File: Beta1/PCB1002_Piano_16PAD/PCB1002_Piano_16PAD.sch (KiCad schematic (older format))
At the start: 40 parts, among them U1 MPR121OTS, U2 MPR121OTS, U3 MPR121OTS

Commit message: Removed Kludge connections. Added MPR121 parts. Reannotated.
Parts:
- removed +3.3VA0, +3.3VB0, +3.3VC0, GNDA0, GNDB0, GNDC0, IRQA0, IRQB0, IRQC0, SCLA0, SCLB0, SCLC0, SDAA0, SDAB0, SDAC0: CONN_01X01, Liberry:single_0.1, symbol CONN_01X01
- removed U1, U2, U3: MPR121OTS, Liberry:MPR121OTS, symbol MPR121OTS
- added C1 (x2), C101: CC0603KRX7R9BB104, Capacitors_SMD:C_0603, symbol C
- added C102, C2 (x2): 0.1uf, Capacitors_SMD:C_0603, symbol C
- added P00, P01, P02, P03, P04, P05, P06, P07, P08, P09, P10, P100, P101, P102, P103, P104, P105, P106, P107, P108, P109, P11, P110, P111, P200, P201, P202, P203, P204, P205, P206, P207, P208, P209, P210, P211: CONN_01X01, Liberry:TESTPAD, symbol CONN_01X01
- added R1 (x2), R101: 75K, Resistors_SMD:R_0603, symbol R
- added R102, R2 (x2): 100K, Resistors_SMD:R_0603, symbol R
- added R? (x3): 10K, Resistors_SMD:R_0603, symbol R
- added U1, U100, U200: MPR121QR2, Liberry:QFN-20-1EP_3x3mm_Pitch0.40mm, symbol MPR121QR2
- +3.3V0, GND0, IRQ0, SCL0, SDA0: footprint Liberry:single_0.1 -> Liberry:TH_0.1_1x2_Jumper
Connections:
- wire segments 89 -> 211
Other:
- moved on the sheet: GND0, IRQ0, PAD0, PAD1, PAD100, PAD101, PAD102, PAD103, PAD104, PAD105, PAD106, PAD107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

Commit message: Fixed dupe annotations
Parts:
- gave numbers to parts that had none: 3
- renumbered C1 to C201, C2 to C202, P00 to P0, P01 to P1, P02 to P2, P03 to P3, P04 to P4, P05 to P5, P06 to P6, P07 to P7, P08 to P8, P09 to P9, R1 to R201, R2 to R202
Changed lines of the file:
@@
 $EndComp
 $Comp
-L GND #PWR?
+L GND #PWR03
 U 1 1 588AAA39
 P 16200 6500
-F 0 "#PWR?" H 16200 6250 50  0001 C CNN
+F 0 "#PWR03" H 16200 6250 50  0001 C CNN
 F 1 "GND" H 16200 6350 50  0000 C CNN
 F 2 "" H 16200 6500 50  0000 C CNN
@@
 $EndComp
 $Comp
-L GND #PWR?
+L GND #PWR04
 U 1 1 588AAA3F
 P 15650 3400
-F 0 "#PWR?" H 15650 3150 50  0001 C CNN
+F 0 "#PWR04" H 15650 3150 50  0001 C CNN
 F 1 "GND" H 15650 3250 50  0000 C CNN
 F 2 "" H 15650 3400 50  0000 C CNN
@@
 $EndComp
 $Comp
-L +3.3V #PWR?
+L +3.3V #PWR05
 U 1 1 588AAA4E
 P 15950 2300
-F 0 "#PWR?" H 15950 2150 50  0001 C CNN
+F 0 "#PWR05" H 15950 2150 50  0001 C CNN
 F 1 "+3.3V" H 15950 2440 50  0000 C CNN
 F 2 "" H 15950 2300 50  0000 C CNN
@@
 $EndComp
 $Comp
-L GND #PWR?
+L GND #PWR06
 U 1 1 588AAA54
 P 15950 2750
-F 0 "#PWR?" H 15950 2500 50  0001 C CNN
+F 0 "#PWR06" H 15950 2500 50  0001 C CNN
 F 1 "GND" H 15950 2600 50  0000 C CNN
 F 2 "" H 15950 2750 50  0000 C CNN
@@
 $EndComp
 $Comp
-L R R?
+L R R301
 U 1 1 588AAA83
 P 4500 2650
-F 0 "R?" V 4580 2650 50  0000 C CNN
+F 0 "R301" V 4580 2650 50  0000 C CNN
 F 1 "10K" V 4500 2650 50  0000 C CNN
 F 2 "Resistors_SMD:R_0603" V 4430 2650 50  0001 C CNN
@@
 $EndComp
 $Comp
-L +3.3V #PWR?
+L +3.3V #PWR07
 U 1 1 588AAA8A
 P 4500 2300
-F 0 "#PWR?" H 4500 2150 50  0001 C CNN
+F 0 "#PWR07" H 4500 2150 50  0001 C CNN
 F 1 "+3.3V" H 4500 2440 50  0000 C CNN
 F 2 "" H 4500 2300 50  0000 C CNN
@@
 $EndComp
 $Comp
-L R R?
+L R R302
 U 1 1 588AAA92
 P 4800 2650
-F 0 "R?" V 4880 2650 50  0000 C CNN
+F 0 "R302" V 4880 2650 50  0000 C CNN
 F 1 "10K" V 4800 2650 50  0000 C CNN
 F 2 "Resistors_SMD:R_0603" V 4730 2650 50  0001 C CNN
@@
 $EndComp
 $Comp
-L +3.3V #PWR?
+L +3.3V #PWR08
 U 1 1 588AAA99
 P 4800 2300
-F 0 "#PWR?" H 4800 2150 50  0001 C CNN
+F 0 "#PWR08" H 4800 2150 50  0001 C CNN
 F 1 "+3.3V" H 4800 2440 50  0000 C CNN
 F 2 "" H 4800 2300 50  0000 C CNN
@@
 $EndComp
 $Comp
-L GND #PWR?
+L GND #PWR09
 U 1 1 588B345D
 P 16150 12500
-F 0 "#PWR?" H 16150 12250 50  0001 C CNN
+F 0 "#PWR09" H 16150 12250 50  0001 C CNN
 F 1 "GND" H 16150 12350 50  0000 C CNN
 F 2 "" H 16150 12500 50  0000 C CNN
@@
 $EndComp
 $Comp
-L GND #PWR?
+L GND #PWR010
 U 1 1 588B3463
 P 15600 9400
-F 0 "#PWR?" H 15600 9150 50  0001 C CNN
+F 0 "#PWR010" H 15600 9150 50  0001 C CNN
 F 1 "GND" H 15600 9250 50  0000 C CNN
 F 2 "" H 15600 9400 50  0000 C CNN
@@
 $EndComp
 $Comp
-L +3.3V #PWR?
+L +3.3V #PWR011
 U 1 1 588B3471
 P 15900 8300
-F 0 "#PWR?" H 15900 8150 50  0001 C CNN
+F 0 "#PWR011" H 15900 8150 50  0001 C CNN
 F 1 "+3.3V" H 15900 8440 50  0000 C CNN
 F 2 "" H 15900 8300 50  0000 C CNN
@@
 $EndComp
 $Comp
-L GND #PWR?
+L GND #PWR012
 U 1 1 588B3477
 P 15900 8750
-F 0 "#PWR?" H 15900 8500 50  0001 C CNN
+F 0 "#PWR012" H 15900 8500 50  0001 C CNN
 F 1 "GND" H 15900 8600 50  0000 C CNN
 F 2 "" H 15900 8750 50  0000 C CNN
@@
 	16350 9800 15800 9800
 $Comp
-L R R2
+L R R202
 U 1 1 588B3AE7
 P 16000 17100
-F 0 "R2" V 16080 17100 50  0000 C CNN
+F 0 "R202" V 16080 17100 50  0000 C CNN
 F 1 "100K" V 16000 17100 50  0000 C CNN
 F 2 "Resistors_SMD:R_0603" V 15930 17100 50  0001 C CNN
@@
 $EndComp
 $Comp
-L R R1
+L R R201
 U 1 1 588B3AEF
 P 16200 17550
-F 0 "R1" V 16280 17550 50  0000 C CNN
+F 0 "R201" V 16280 17550 50  0000 C CNN
 F 1 "75K" V 16200 17550 50  0000 C CNN
 F 2 "Resistors_SMD:R_0603" V 16130 17550 50  0001 C CNN
@@
 $EndComp
 $Comp
-L C C2
+L C C202
 U 1 1 588B3AF7
 P 15550 14600
-F 0 "C2" H 15575 14700 50  0000 L CNN
+F 0 "C202" H 15575 14700 50  0000 L CNN
 F 1 "0.1uf" H 15575 14500 50  0000 L CNN
 F 2 "Capacitors_SMD:C_0603" H 15588 14450 50  0001 C CNN
@@
 $EndComp
 $Comp
-L GND #PWR?
+L GND #PWR013
 U 1 1 588B3AFD
 P 16100 17950
-F 0 "#PWR?" H 16100 17700 50  0001 C CNN
+F 0 "#PWR013" H 16100 17700 50  0001 C CNN
 F 1 "GND" H 16100 17800 50  0000 C CNN
 F 2 "" H 16100 17950 50  0000 C CNN
@@
 $EndComp
 $Comp
-L GND #PWR?
+L GND #PWR014
 U 1 1 588B3B03
 P 15550 14850
-F 0 "#PWR?" H 15550 14600 50  0001 C CNN
+F 0 "#PWR014" H 15550 14600 50  0001 C CNN
 F 1 "GND" H 15550 14700 50  0000 C CNN
 F 2 "" H 15550 14850 50  0000 C CNN
@@
 $EndComp
 $Comp
-L C C1
+L C C201
 U 1 1 588B3B0B
 P 15850 13950
-F 0 "C1" H 15875 14050 50  0000 L CNN
+F 0 "C201" H 15875 14050 50  0000 L CNN
 F 1 "CC0603KRX7R9BB104" H 15875 13850 50  0000 L CNN
 F 2 "Capacitors_SMD:C_0603" H 15888 13800 50  0001 C CNN
@@
 $EndComp
 $Comp
-L +3.3V #PWR?
+L +3.3V #PWR015
 U 1 1 588B3B11
 P 15850 13750
-F 0 "#PWR?" H 15850 13600 50  0001 C CNN
+F 0 "#PWR015" H 15850 13600 50  0001 C CNN
 F 1 "+3.3V" H 15850 13890 50  0000 C CNN
 F 2 "" H 15850 13750 50  0000 C CNN
@@
 $EndComp
 $Comp
-L GND #PWR?
+L GND #PWR016
 U 1 1 588B3B17
 P 15850 14200
-F 0 "#PWR?" H 15850 13950 50  0001 C CNN
+F 0 "#PWR016" H 15850 13950 50  0001 C CNN
 F 1 "GND" H 15850 14050 50  0000 C CNN
 F 2 "" H 15850 14200 50  0000 C CNN
@@
 	16300 15250 15750 15250
 $Comp
-L CONN_01X01 P00
+L CONN_01X01 P0
 U 1 1 588B8F4E
 P 13600 5600
-F 0 "P00" H 13850 5600 50  0000 C CNN
+F 0 "P0" H 13850 5600 50  0000 C CNN
 F 1 "CONN_01X01" V 13700 5600 50  0001 C CNN
 F 2 "Liberry:TESTPAD" H 13600 5600 50  0001 C CNN
@@
 $EndComp
 $Comp
-L CONN_01X01 P01
+L CONN_01X01 P1
 U 1 1 588BA8DA
 P 13600 5700
-F 0 "P01" H 13850 5700 50  0000 C CNN
+F 0 "P1" H 13850 5700 50  0000 C CNN
 F 1 "CONN_01X01" V 13700 5700 50  0001 C CNN
 F 2 "Liberry:TESTPAD" H 13600 5700 50  0001 C CNN
@@
 $EndComp
 $Comp
-L CONN_01X01 P02
+L CONN_01X01 P2
 U 1 1 588BA97E
 P 13600 5800
-F 0 "P02" H 13850 5800 50  0000 C CNN
+F 0 "P2" H 13850 5800 50  0000 C CNN
 F 1 "CONN_01X01" V 13700 5800 50  0001 C CNN
 F 2 "Liberry:TESTPAD" H 13600 5800 50  0001 C CNN
@@
 $EndComp
 $Comp
-L CONN_01X01 P03
+L CONN_01X01 P3
 U 1 1 588BAA25
 P 13600 5900
-F 0 "P03" H 13850 5900 50  0000 C CNN
+F 0 "P3" H 13850 5900 50  0000 C CNN
 F 1 "CONN_01X01" V 13700 5900 50  0001 C CNN
 F 2 "Liberry:TESTPAD" H 13600 5900 50  0001 C CNN
@@
 $EndComp
 $Comp
-L CONN_01X01 P04
+L CONN_01X01 P4
 U 1 1 588BAAD1
 P 13600 6000
-F 0 "P04" H 13850 6000 50  0000 C CNN
+F 0 "P4" H 13850 6000 50  0000 C CNN
 F 1 "CONN_01X01" V 13700 6000 50  0001 C CNN
 F 2 "Liberry:TESTPAD" H 13600 6000 50  0001 C CNN
@@
 $EndComp
 $Comp
-L CONN_01X01 P05
+L CONN_01X01 P5
 U 1 1 588BAB7E
 P 13600 6100
-F 0 "P05" H 13850 6100 50  0000 C CNN
+F 0 "P5" H 13850 6100 50  0000 C CNN
 F 1 "CONN_01X01" V 13700 6100 50  0001 C CNN
 F 2 "Liberry:TESTPAD" H 13600 6100 50  0001 C CNN
@@
 $EndComp
 $Comp
-L CONN_01X01 P06
+L CONN_01X01 P6
 U 1 1 588BAC32
 P 13600 6200
-F 0 "P06" H 13850 6200 50  0000 C CNN
+F 0 "P6" H 13850 6200 50  0000 C CNN
 F 1 "CONN_01X01" V 13700 6200 50  0001 C CNN
 F 2 "Liberry:TESTPAD" H 13600 6200 50  0001 C CNN
@@
 $EndComp
 $Comp
-L CONN_01X01 P07
+L CONN_01X01 P7
 U 1 1 588BACE7
 P 13600 6300
-F 0 "P07" H 13850 6300 50  0000 C CNN
+F 0 "P7" H 13850 6300 50  0000 C CNN
 F 1 "CONN_01X01" V 13700 6300 50  0001 C CNN
 F 2 "Liberry:TESTPAD" H 13600 6300 50  0001 C CNN
@@
 $EndComp
 $Comp
-L CONN_01X01 P08
+L CONN_01X01 P8
 U 1 1 588BAD9D
 P 13600 6400
-F 0 "P08" H 13850 6400 50  0000 C CNN
+F 0 "P8" H 13850 6400 50  0000 C CNN
 F 1 "CONN_01X01" V 13700 6400 50  0001 C CNN
 F 2 "Liberry:TESTPAD" H 13600 6400 50  0001 C CNN
@@
 $EndComp
 $Comp
-L CONN_01X01 P09
+L CONN_01X01 P9
 U 1 1 588BAE5A
 P 13600 6500
-F 0 "P09" H 13850 6500 50  0000 C CNN
+F 0 "P9" H 13850 6500 50  0000 C CNN
 F 1 "CONN_01X01" V 13700 6500 50  0001 C CNN
 F 2 "Liberry:TESTPAD" H 13600 6500 50  0001 C CNN
@@
 Connection ~ 16100 17800
 $Comp
-L +3.3V #PWR?
+L +3.3V #PWR017
 U 1 1 588C861E
 P 15800 11650
-F 0 "#PWR?" H 15800 11500 50  0001 C CNN
+F 0 "#PWR017" H 15800 11500 50  0001 C CNN
 F 1 "+3.3V" H 15800 11790 50  0000 C CNN
 F 2 "" H 15800 11650 50  0000 C CNN
@@
 	18450 9250 19100 9250
 $Comp
-L R R?
+L R R303
 U 1 1 588CC72E
 P 5150 2650
-F 0 "R?" V 5230 2650 50  0000 C CNN
+F 0 "R303" V 5230 2650 50  0000 C CNN
 F 1 "10K" V 5150 2650 50  0000 C CNN
 F 2 "Resistors_SMD:R_0603" V 5080 2650 50  0001 C CNN
@@
 $EndComp
 $Comp
-L +3.3V #PWR?
+L +3.3V #PWR018
 U 1 1 588CC734
 P 5150 2300
-F 0 "#PWR?" H 5150 2150 50  0001 C CNN
+F 0 "#PWR018" H 5150 2150 50  0001 C CNN
 F 1 "+3.3V" H 5150 2440 50  0000 C CNN
 F 2 "" H 5150 2300 50  0000 C CNN

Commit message: Placement Done.
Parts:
- added A0, A1, A2, A3, A4, A5: CONN_01X01, Liberry:TH_0.1_1x2_Jumper, symbol CONN_01X01
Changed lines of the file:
@@
 	16150 4050 16150 3800
 Connection ~ 16150 3800
+$Comp
+L CONN_01X01 A0
+U 1 1 588F39C7
+P 3850 5150
+F 0 "A0" H 4200 5150 50  0000 R CNN
+F 1 "CONN_01X01" V 3950 5150 50  0001 C CNN
+F 2 "Liberry:TH_0.1_1x2_Jumper" H 3850 5150 50  0001 C CNN
+F 3 "" H 3850 5150 50  0000 C CNN
+F 4 "PCB" H 3850 5150 60  0001 C CNN "MFG"
+F 5 "ON_PCB" H 3850 5150 60  0001 C CNN "MPN"
+	1    3850 5150
+	-1   0    0    1
+$EndComp
+$Comp
+L CONN_01X01 A1
+U 1 1 588F3BC4
+P 3850 5300
+F 0 "A1" H 4200 5300 50  0000 R CNN
+F 1 "CONN_01X01" V 3950 5300 50  0001 C CNN
+F 2 "Liberry:TH_0.1_1x2_Jumper" H 3850 5300 50  0001 C CNN
+F 3 "" H 3850 5300 50  0000 C CNN
+F 4 "PCB" H 3850 5300 60  0001 C CNN "MFG"
+F 5 "ON_PCB" H 3850 5300 60  0001 C CNN "MPN"
+	1    3850 5300
+	-1   0    0    1
+$EndComp
+$Comp
+L CONN_01X01 A2
+U 1 1 588F3E53
+P 3850 5450
+F 0 "A2" H 4200 5450 50  0000 R CNN
+F 1 "CONN_01X01" V 3950 5450 50  0001 C CNN
+F 2 "Liberry:TH_0.1_1x2_Jumper" H 3850 5450 50  0001 C CNN
+F 3 "" H 3850 5450 50  0000 C CNN
+F 4 "PCB" H 3850 5450 60  0001 C CNN "MFG"
+F 5 "ON_PCB" H 3850 5450 60  0001 C CNN "MPN"
+	1    3850 5450
+	-1   0    0    1
+$EndComp
+$Comp
+L CONN_01X01 A3
+U 1 1 588F404A
+P 3850 5600
+F 0 "A3" H 4200 5600 50  0000 R CNN
+F 1 "CONN_01X01" V 3950 5600 50  0001 C CNN
+F 2 "Liberry:TH_0.1_1x2_Jumper" H 3850 5600 50  0001 C CNN
+F 3 "" H 3850 5600 50  0000 C CNN
+F 4 "PCB" H 3850 5600 60  0001 C CNN "MFG"
+F 5 "ON_PCB" H 3850 5600 60  0001 C CNN "MPN"
+	1    3850 5600
+	-1   0    0    1
+$EndComp
+$Comp
+L CONN_01X01 A4
+U 1 1 588F4154
+P 3850 5750
+F 0 "A4" H 4200 5750 50  0000 R CNN
+F 1 "CONN_01X01" V 3950 5750 50  0001 C CNN
+F 2 "Liberry:TH_0.1_1x2_Jumper" H 3850 5750 50  0001 C CNN
+F 3 "" H 3850 5750 50  0000 C CNN
+F 4 "PCB" H 3850 5750 60  0001 C CNN "MFG"
+F 5 "ON_PCB" H 3850 5750 60  0001 C CNN "MPN"
+	1    3850 5750
+	-1   0    0    1
+$EndComp
+$Comp
+L CONN_01X01 A5
+U 1 1 588F4263
+P 3850 5900
+F 0 "A5" H 4200 5900 50  0000 R CNN
+F 1 "CONN_01X01" V 3950 5900 50  0001 C CNN
+F 2 "Liberry:TH_0.1_1x2_Jumper" H 3850 5900 50  0001 C CNN
+F 3 "" H 3850 5900 50  0000 C CNN
+F 4 "PCB" H 3850 5900 60  0001 C CNN "MFG"
+F 5 "ON_PCB" H 3850 5900 60  0001 C CNN "MPN"
+	1    3850 5900
+	-1   0    0    1
+$EndComp
 $EndSCHEMATC

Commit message: Done routing.
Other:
- note added: "NRFND"
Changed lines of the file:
@@
 	-1   0    0    1
 $EndComp
+Text Notes 17700 6400 0    60   ~ 0
+NRFND
+Text Notes 17650 12400 0    60   ~ 0
+NRFND
+Text Notes 17600 17850 0    60   ~ 0
+NRFND
 $EndSCHEMATC

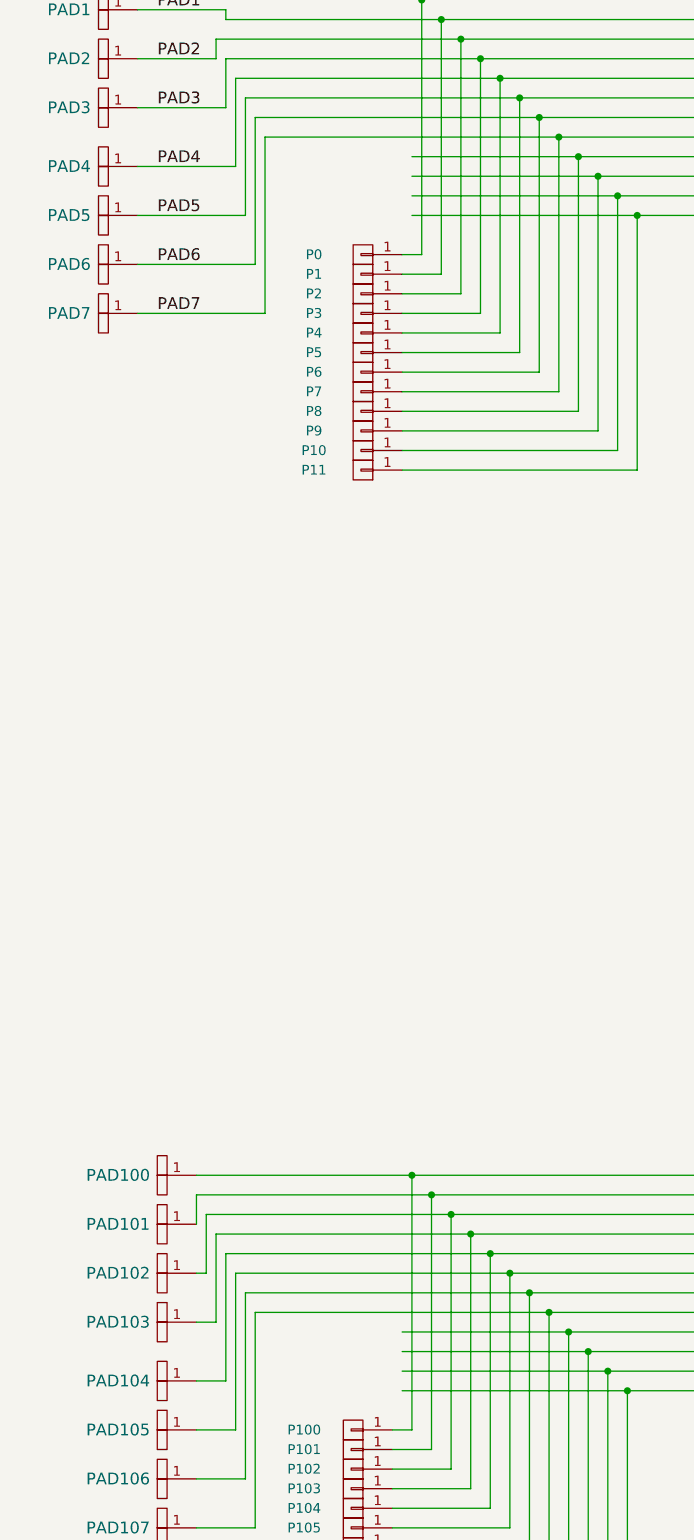
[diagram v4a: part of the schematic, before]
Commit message: Added surplus padcap signal access to mezzanine
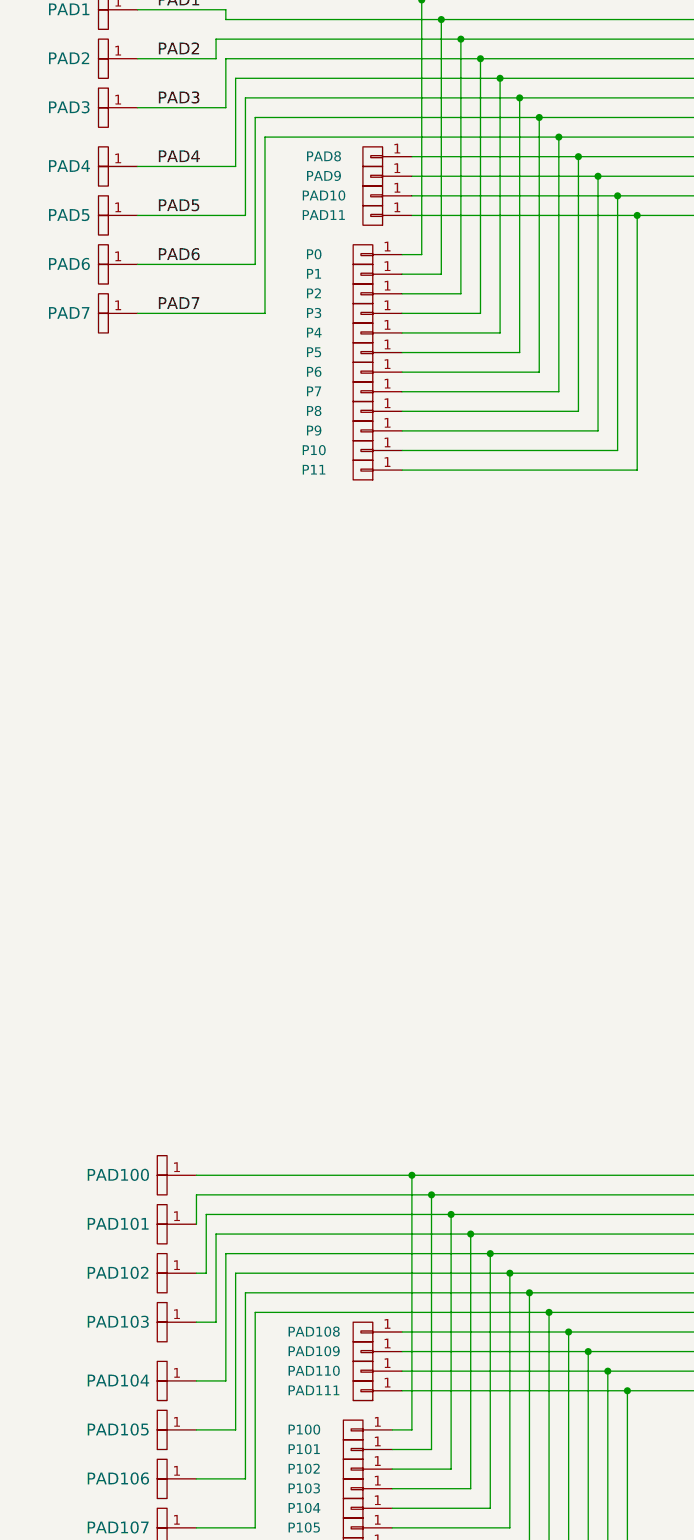
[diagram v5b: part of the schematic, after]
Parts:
- added PAD10, PAD108, PAD109, PAD11, PAD110, PAD111, PAD8, PAD9: CONN_01X01, Liberry:single_0.1, symbol CONN_01X01
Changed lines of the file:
@@
 Text Notes 17600 17850 0    60   ~ 0
 NRFND
+$Comp
+L CONN_01X01 PAD8
+U 1 1 588AF5E8
+P 13650 5100
+F 0 "PAD8" H 13900 5100 50  0000 C CNN
+F 1 "CONN_01X01" V 13750 5100 50  0001 C CNN
+F 2 "Liberry:single_0.1" H 13650 5100 50  0001 C CNN
+F 3 "" H 13650 5100 50  0000 C CNN
+F 4 "PCB" H 13650 5100 60  0001 C CNN "MFG"
+F 5 "ON_PCB" H 13650 5100 60  0001 C CNN "MPN"
+	1    13650 5100
+	-1   0    0    1
+$EndComp
+$Comp
+L CONN_01X01 PAD9
+U 1 1 588B08B7
+P 13650 5200
+F 0 "PAD9" H 13900 5200 50  0000 C CNN
+F 1 "CONN_01X01" V 13750 5200 50  0001 C CNN
+F 2 "Liberry:single_0.1" H 13650 5200 50  0001 C CNN
+F 3 "" H 13650 5200 50  0000 C CNN
+F 4 "PCB" H 13650 5200 60  0001 C CNN "MFG"
+F 5 "ON_PCB" H 13650 5200 60  0001 C CNN "MPN"
+	1    13650 5200
+	-1   0    0    1
+$EndComp
+$Comp
+L CONN_01X01 PAD10
+U 1 1 588B09C7
+P 13650 5300
+F 0 "PAD10" H 13900 5300 50  0000 C CNN
+F 1 "CONN_01X01" V 13750 5300 50  0001 C CNN
+F 2 "Liberry:single_0.1" H 13650 5300 50  0001 C CNN
+F 3 "" H 13650 5300 50  0000 C CNN
+F 4 "PCB" H 13650 5300 60  0001 C CNN "MFG"
+F 5 "ON_PCB" H 13650 5300 60  0001 C CNN "MPN"
+	1    13650 5300
+	-1   0    0    1
+$EndComp
+$Comp
+L CONN_01X01 PAD11
+U 1 1 588B0ADA
+P 13650 5400
+F 0 "PAD11" H 13900 5400 50  0000 C CNN
+F 1 "CONN_01X01" V 13750 5400 50  0001 C CNN
+F 2 "Liberry:single_0.1" H 13650 5400 50  0001 C CNN
+F 3 "" H 13650 5400 50  0000 C CNN
+F 4 "PCB" H 13650 5400 60  0001 C CNN "MFG"
+F 5 "ON_PCB" H 13650 5400 60  0001 C CNN "MPN"
+	1    13650 5400
+	-1   0    0    1
+$EndComp
+$Comp
+L CONN_01X01 PAD108
+U 1 1 588B2E3E
+P 13600 11100
+F 0 "PAD108" H 13850 11100 50  0000 C CNN
+F 1 "CONN_01X01" V 13700 11100 50  0001 C CNN
+F 2 "Liberry:single_0.1" H 13600 11100 50  0001 C CNN
+F 3 "" H 13600 11100 50  0000 C CNN
+F 4 "PCB" H 13600 11100 60  0001 C CNN "MFG"
+F 5 "ON_PCB" H 13600 11100 60  0001 C CNN "MPN"
+	1    13600 11100
+	-1   0    0    1
+$EndComp
+$Comp
+L CONN_01X01 PAD109
+U 1 1 588B3696
+P 13600 11200
+F 0 "PAD109" H 13850 11200 50  0000 C CNN
+F 1 "CONN_01X01" V 13700 11200 50  0001 C CNN
+F 2 "Liberry:single_0.1" H 13600 11200 50  0001 C CNN
+F 3 "" H 13600 11200 50  0000 C CNN
+F 4 "PCB" H 13600 11200 60  0001 C CNN "MFG"
+F 5 "ON_PCB" H 13600 11200 60  0001 C CNN "MPN"
+	1    13600 11200
+	-1   0    0    1
+$EndComp
+$Comp
+L CONN_01X01 PAD110
+U 1 1 588B37B2
+P 13600 11300
+F 0 "PAD110" H 13850 11300 50  0000 C CNN
+F 1 "CONN_01X01" V 13700 11300 50  0001 C CNN
+F 2 "Liberry:single_0.1" H 13600 11300 50  0001 C CNN
+F 3 "" H 13600 11300 50  0000 C CNN
+F 4 "PCB" H 13600 11300 60  0001 C CNN "MFG"
+F 5 "ON_PCB" H 13600 11300 60  0001 C CNN "MPN"
+	1    13600 11300
+	-1   0    0    1
+$EndComp
+$Comp
+L CONN_01X01 PAD111
+U 1 1 588B38D1
+P 13600 11400
+F 0 "PAD111" H 13850 11400 50  0000 C CNN
+F 1 "CONN_01X01" V 13700 11400 50  0001 C CNN
+F 2 "Liberry:single_0.1" H 13600 11400 50  0001 C CNN
+F 3 "" H 13600 11400 50  0000 C CNN
+F 4 "PCB" H 13600 11400 60  0001 C CNN "MFG"
+F 5 "ON_PCB" H 13600 11400 60  0001 C CNN "MPN"
+	1    13600 11400
+	-1   0    0    1
+$EndComp
 $EndSCHEMATC
